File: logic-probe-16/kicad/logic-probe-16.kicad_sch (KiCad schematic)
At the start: 10 parts, among them J1 Conn_01x02_Pin, U1 LM339

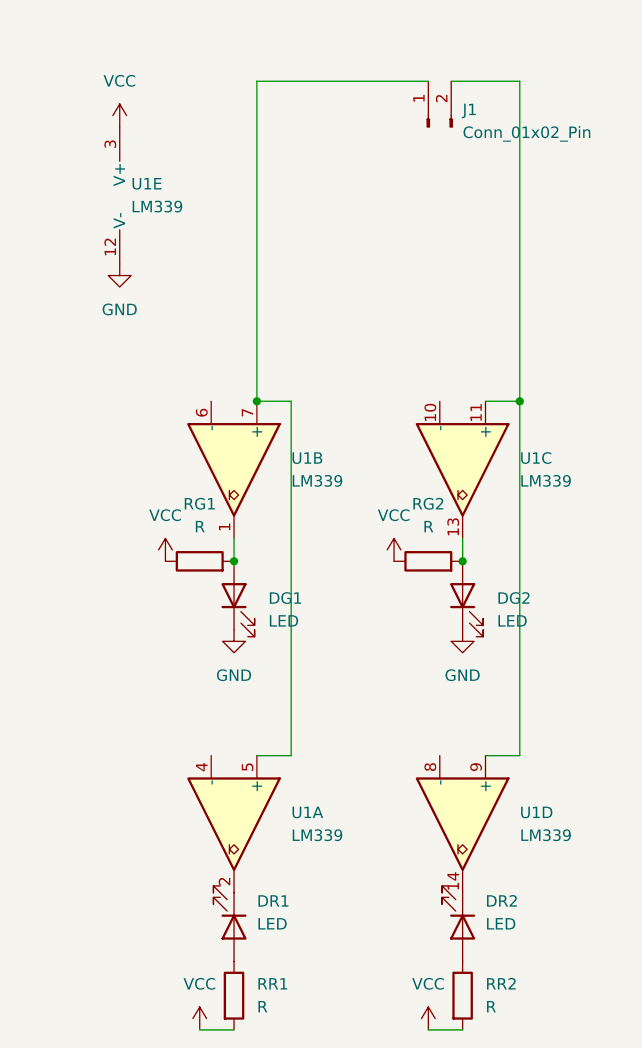
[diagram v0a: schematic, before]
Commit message: WIP logic-probe-16 sch: Fix LEDs; add input resistors
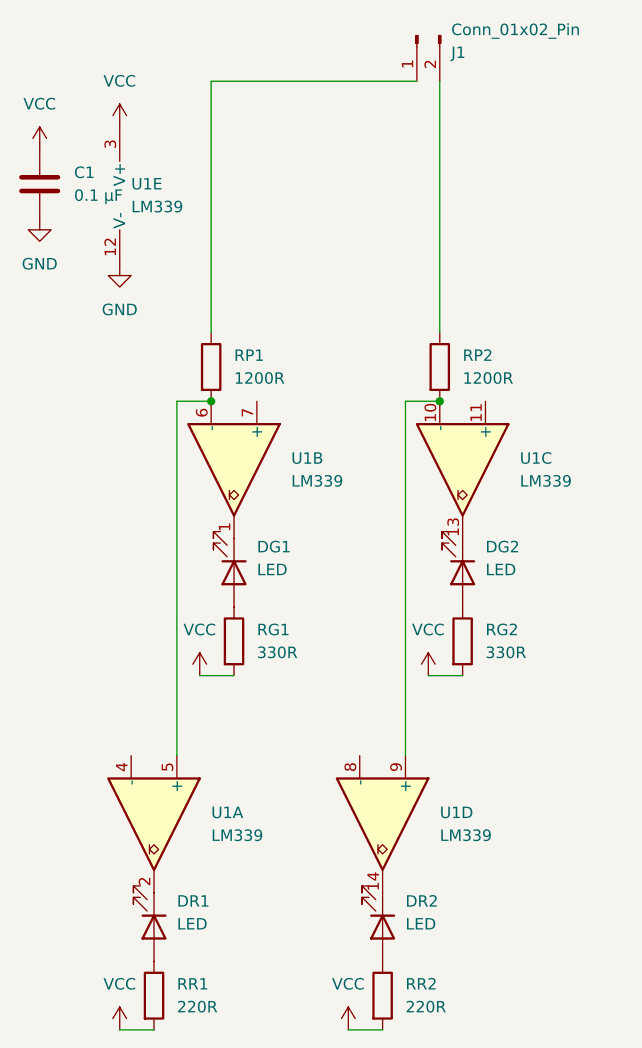
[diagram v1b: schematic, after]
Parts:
- added C1: 0.1 μF, symbol Device:C
- added RP1, RP2: 1200R, symbol Device:R
- DG1, DG2: footprint (none) -> LED_SMD:LED_1206_3216Metric
- RG1, RG2: value R -> 330R; footprint (none) -> Resistor_SMD:R_0805_2012Metric
- RR1, RR2: value R -> 220R
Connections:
- net GND: now also C1.2; no longer DG1.1 (K), DG2.1 (K)
- net VCC: now also RG1.2, RG2.2, C1.1; no longer RG1.1, RG2.1
- net at U1.6 (-): now also U1.5 (+), RP1.2
- net at U1.10 (-): now also U1.9 (+), RP2.2
- new net: DG1.1 (K), U1.1
- new net: DG1.2 (A), RG1.1
- new net: DG2.1 (K), U1.13
- new net: DG2.2 (A), RG2.1
- new net: J1.1 (Pin_1), RP1.1
- new net: J1.2 (Pin_2), RP2.1
- now unconnected: U1.11 (+), U1.7 (+)
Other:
- moved on the sheet: DR1, DR2, J1, RR1, RR2, U1A, U1D
